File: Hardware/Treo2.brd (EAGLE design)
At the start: 8 parts

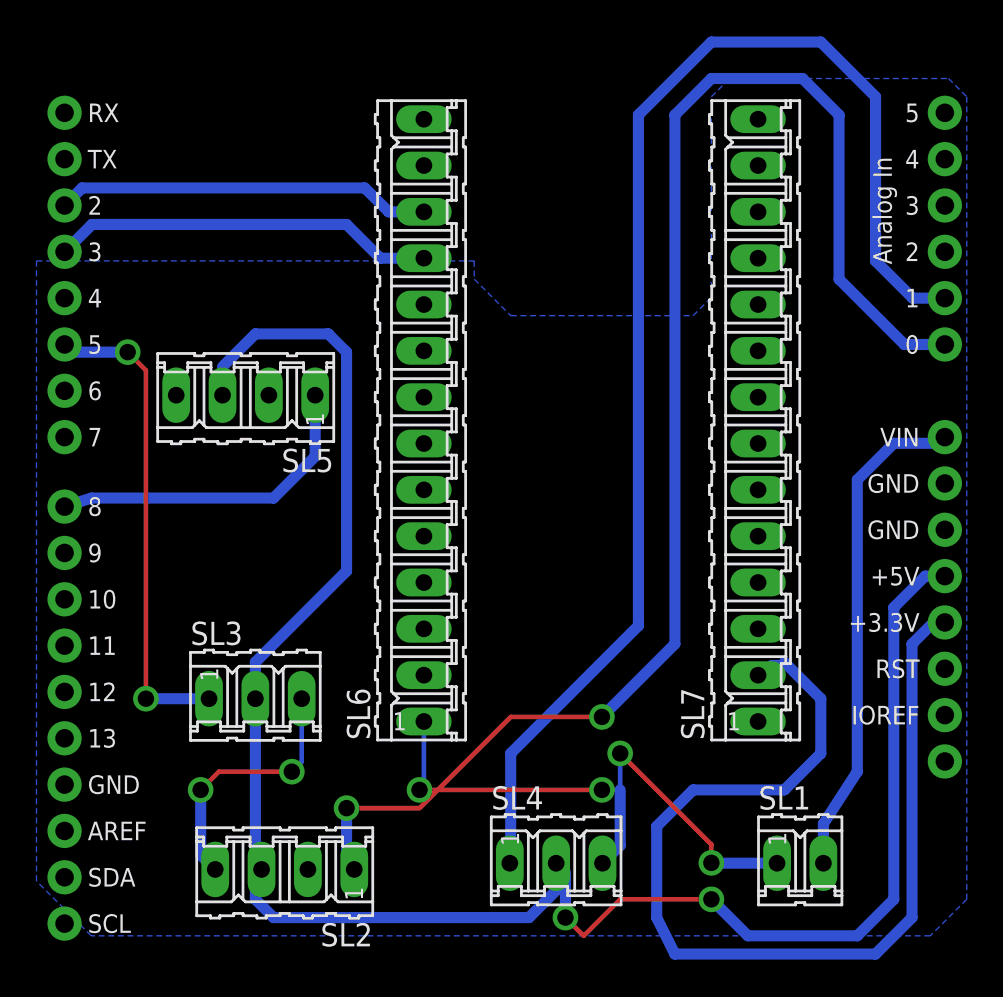
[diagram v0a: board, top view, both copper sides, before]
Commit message: add cnc gcode & designs/code for docking station
Change-Id: I07bf7ad853945ddfc4129ba2e5f8d283fc952889
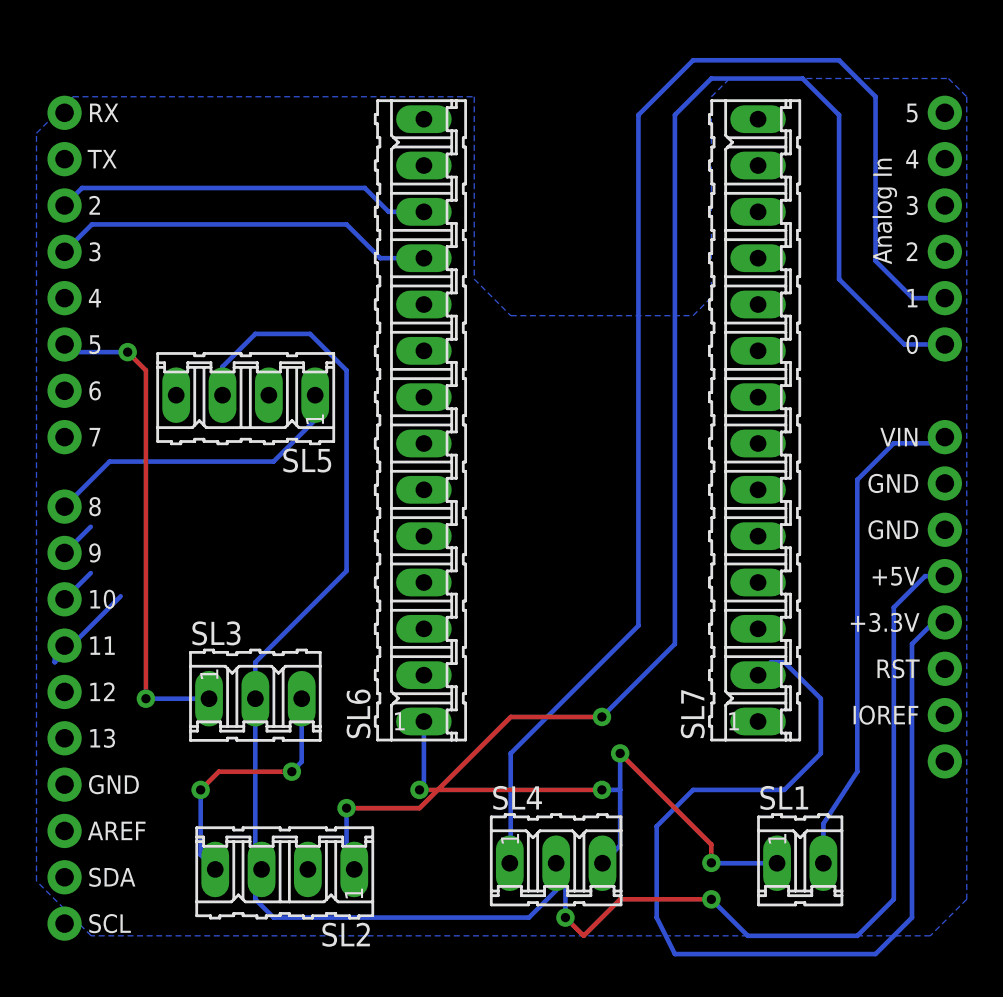
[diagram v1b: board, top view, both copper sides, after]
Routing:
- net D11: track 0.00 -> 6.25 mm
- net D9: track 0.00 -> 2.03 mm
- net D10: track 0.00 -> 2.03 mm
- net D8: track 18.1 -> 17.1 mm
- net A1: track 73.5 -> 72.7 mm
- net 5V: track 104.5 -> 103.9 mm
